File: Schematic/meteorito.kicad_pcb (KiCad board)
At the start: 2 copper layers, 95.3 x 89.4 mm, 17 parts, among them P1 DH22, P10 CONN_01X10, P2 GY-ML8511, P3 BMP180, P4 Hall, P5 Hall, P6 Hall, P7 CONN_01X10, P8 CONN_01X10, P9 CONN_01X10

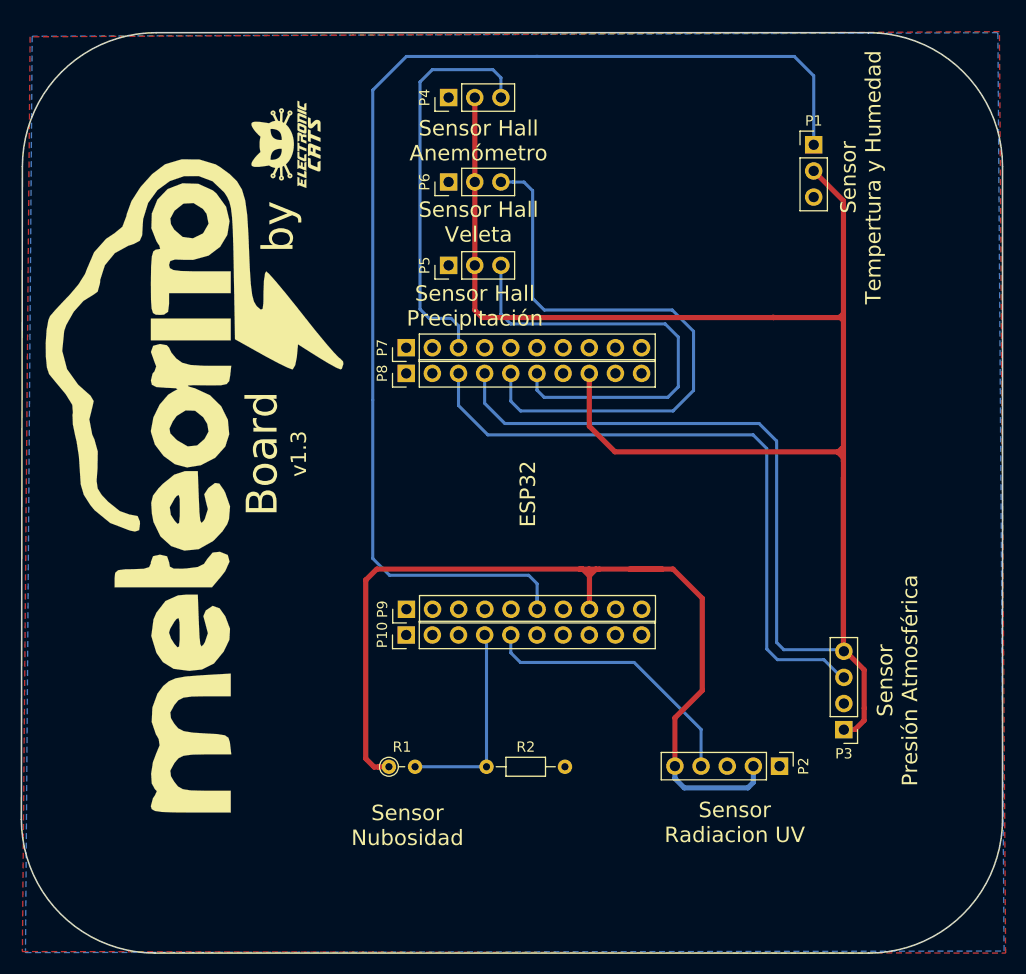
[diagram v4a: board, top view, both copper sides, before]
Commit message: Add library update components and layout
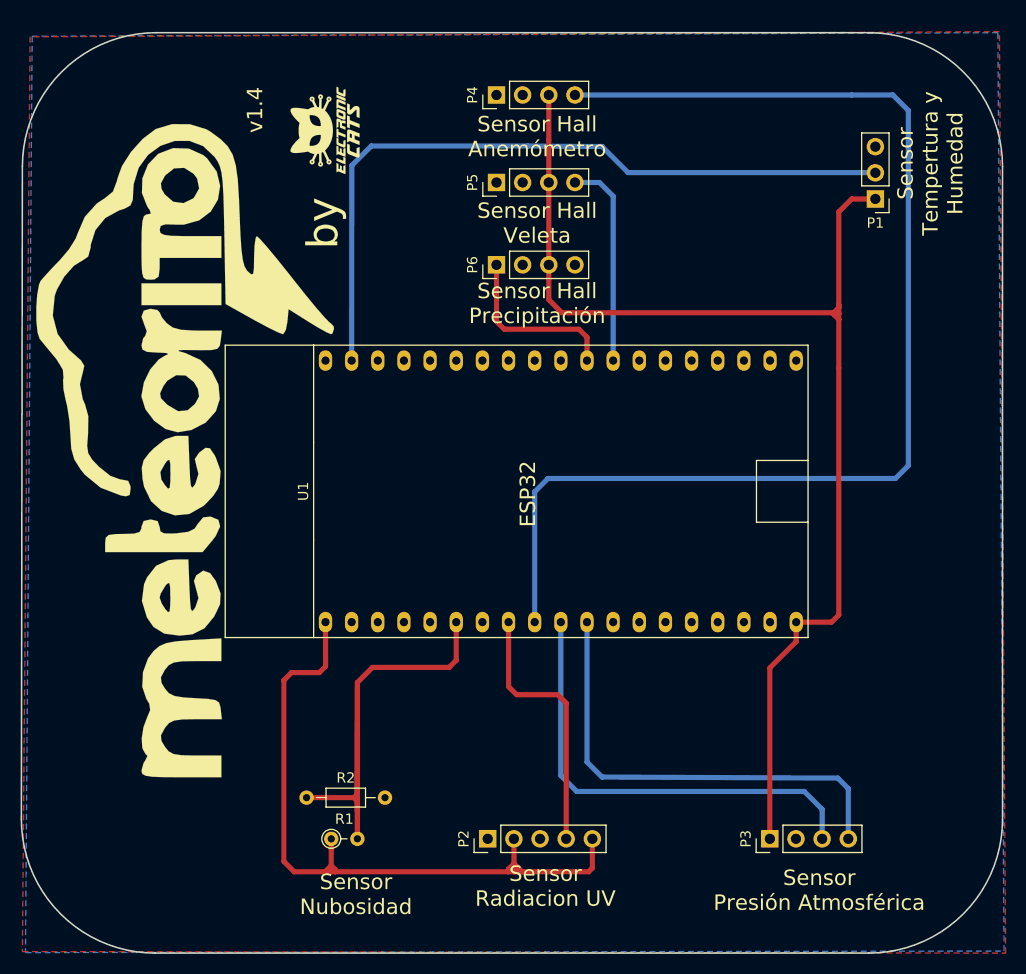
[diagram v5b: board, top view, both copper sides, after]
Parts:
- removed P10, P7, P8, P9: CONN_01X10, Connector_PinHeader_2.54mm:PinHeader_1x10_P2.54mm_Vertical
- added U1: ESP32-DEVKIT, meteorito:ESP32-DEVKIT, F.Cu at (92.1, 100.2)
- P4: value Hall -> Velocidad; footprint Connector_PinHeader_2.54mm:PinHeader_1x03_P2.54mm_Vertical -> Connector_PinHeader_2.54mm:PinHeader_1x04_P2.54mm_Vertical
- P5, P6: value Hall -> Precipitacion; footprint Connector_PinHeader_2.54mm:PinHeader_1x03_P2.54mm_Vertical -> Connector_PinHeader_2.54mm:PinHeader_1x04_P2.54mm_Vertical
- moved P2 29.2 mm to (85.0, 134.0), turned to 90 degrees
- moved R2 17.7 mm to (67.4, 130.0)
- moved P3 12.8 mm to (112.4, 134.0), turned to 90 degrees
- moved P5 9.30 mm to (85.8, 70.2)
- moved P6 9.30 mm to (85.8, 78.2)
- moved R1 8.96 mm to (69.8, 134.0)
- moved P1 7.97 mm to (122.7, 71.8), turned to 180 degrees
- moved P4 4.66 mm to (85.8, 61.8)
- moved G*** 4.03 mm to (69.2, 65.2)
- moved G*** 3.54 mm to (55.6, 96.3)
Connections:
- P1 pad 1: /IO23 -> +5V
- P1 pad 2: +5V -> /DHT22
- P2 pad 4: /IO33 -> /UV-SENSOR
- P3 pad 3: /IO22 -> /SCL
- P3 pad 4: /IO21 -> /SDA
- P4 pad 1: GND -> Net-(P4-Pad1)
- P4 pad 2: +5V -> GND
- P4 pad 3: /IO25 -> +5V
- P5 pad 1: GND -> Net-(P5-Pad1)
- P5 pad 2: +5V -> GND
- P5 pad 3: /IO16 -> +5V
- P6 pad 1: GND -> /IO17
- P6 pad 2: +5V -> GND
- P6 pad 3: /IO17 -> +5V
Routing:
- net /IO23: track 118.1 -> 0.00 mm
- net /AIRE-HALL: track 0.00 -> 117.5 mm
- net /DHT22: track 0.00 -> 71.3 mm
- net /IO22: track 62.6 -> 0.00 mm
- net /IO21: track 59.0 -> 0.00 mm
- net /SDA: track 0.00 -> 44.9 mm
- net /SCL: track 0.00 -> 44.5 mm
- net +5V: track 163.2 -> 120.2 mm
- net /IO17: track 58.2 -> 17.2 mm
- net /IO25: track 39.2 -> 0.00 mm
- net /IO35: track 19.8 -> 51.1 mm
- net /IO33: track 26.9 -> 0.00 mm
- net /UV-SENSOR: track 0.00 -> 25.7 mm
- net /IO16: track 43.8 -> 20.2 mm
- net +3V3: track 92.2 -> 70.1 mm
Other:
- net class Default: clearance 0.2 -> 0.4; trace_width 0.3 -> 0.5
- net class Voltaje: clearance 0.2 -> 0.4
- rule trace_clearance: 0.2 -> 0.4
- board text added: "v1.4"
- board text removed: "Board"
- board text removed: "v1.3"

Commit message: Add labels pins
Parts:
- moved G*** 2.16 mm to (127.5, 116.6)
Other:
- board text added: "3V3"
- board text added: "5V"
- board text added: "A0"
- board text added: "D0"
- board text added: "FOTORESISTENCIA"
- board text added: "GND"
- board text added: "NC"
- board text added: "PIN"
- board text added: "SCL"
- board text added: "SDA"
- board text added: "UV"
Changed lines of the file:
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@@
   (general
     (thickness 1.6)
-    (drawings 29)
+    (drawings 53)
     (tracks 103)
     (zones 0)
@@
   )
   (module Aesthetics:hacedores (layer B.Cu)
-    (at 125.349 116.713 270)
+    (at 127.508 116.586 270)
     (fp_text reference G*** (at 0 0 270) (layer B.SilkS) hide
       (effects (font (size 1.524 1.524) (thickness 0.3)) (justify mirror))
@@
       (xy -20.493307 -10.275275) (xy -20.495908 -10.265513)) (layer B.SilkS) (width 0))
   )
+  (gr_text NC (at 85.598 64.008) (layer B.SilkS)
+    (effects (font (size 1 1) (thickness 0.15)) (justify mirror))
+  )
+  (gr_text NC (at 85.598 72.39) (layer B.SilkS)
+    (effects (font (size 1 1) (thickness 0.15)) (justify mirror))
+  )
+  (gr_text NC (at 93.218 80.518) (layer B.SilkS)
+    (effects (font (size 1 1) (thickness 0.15)) (justify mirror))
+  )
+  (gr_text FOTORESISTENCIA (at 71.12 136.398) (layer B.SilkS)
+    (effects (font (size 1 1) (thickness 0.15)) (justify mirror))
+  )
+  (gr_text 3V3 (at 87.63 131.318 90) (layer B.SilkS)
+    (effects (font (size 1 1) (thickness 0.15)) (justify mirror))
+  )
+  (gr_text GND (at 90.17 131.318 90) (layer B.SilkS)
+    (effects (font (size 1 1) (thickness 0.15)) (justify mirror))
+  )
+  (gr_text UV (at 92.71 131.572 90) (layer B.SilkS)
+    (effects (font (size 1 1) (thickness 0.15)) (justify mirror))
+  )
+  (gr_text 3V3 (at 95.25 131.318 90) (layer B.SilkS)
+    (effects (font (size 1 1) (thickness 0.15)) (justify mirror))
+  )
+  (gr_text 5V (at 112.522 131.572 90) (layer B.SilkS)
+    (effects (font (size 1 1) (thickness 0.15)) (justify mirror))
+  )
+  (gr_text GND (at 115.062 131.318 90) (layer B.SilkS)
+    (effects (font (size 1 1) (thickness 0.15)) (justify mirror))
+  )
+  (gr_text SDA (at 119.888 131.064 90) (layer B.SilkS)
+    (effects (font (size 1 1) (thickness 0.15)) (justify mirror))
+  )
+  (gr_text SCL (at 117.348 131.318 90) (layer B.SilkS)
+    (effects (font (size 1 1) (thickness 0.15)) (justify mirror))
+  )
+  (gr_text 5V (at 119.888 71.882) (layer B.SilkS)
+    (effects (font (size 1 1) (thickness 0.15)) (justify mirror))
+  )
+  (gr_text PIN (at 119.888 69.342) (layer B.SilkS)
+    (effects (font (size 1 1) (thickness 0.15)) (justify mirror))
+  )
+  (gr_text GND (at 119.634 66.802) (layer B.SilkS)
+    (effects (font (size 1 1) (thickness 0.15)) (justify mirror))
+  )
+  (gr_text 5V (at 90.932 80.518) (layer B.SilkS)
+    (effects (font (size 1 1) (thickness 0.15)) (justify mirror))
+  )
+  (gr_text GND (at 88.392 80.518) (layer B.SilkS)
+    (effects (font (size 1 1) (thickness 0.15)) (justify mirror))
+  )
+  (gr_text D0 (at 85.852 80.518) (layer B.SilkS)
+    (effects (font (size 1 1) (thickness 0.15)) (justify mirror))
+  )
+  (gr_text GND (at 88.392 72.39) (layer B.SilkS)
+    (effects (font (size 1 1) (thickness 0.15)) (justify mirror))
+  )
+  (gr_text 5V (at 90.932 72.39) (layer B.SilkS)
+    (effects (font (size 1 1) (thickness 0.15)) (justify mirror))
+  )
+  (gr_text A0 (at 93.472 72.39) (layer B.SilkS)
+    (effects (font (size 1 1) (thickness 0.15)) (justify mirror))
+  )
+  (gr_text GND (at 88.392 64.008) (layer B.SilkS)
+    (effects (font (size 1 1) (thickness 0.15)) (justify mirror))
+  )
+  (gr_text 5V (at 90.932 64.008) (layer B.SilkS)
+    (effects (font (size 1 1) (thickness 0.15)) (justify mirror))
+  )
+  (gr_text A0 (at 93.472 64.008) (layer B.SilkS)
+    (effects (font (size 1 1) (thickness 0.15)) (justify mirror))
+  )
   (gr_text "Sensor Hall\nPrecipitación " (at 89.8 82) (layer F.SilkS)
     (effects (font (size 1.5 1.5) (thickness 0.3)))
@@
     (effects (font (size 2.5 2.5) (thickness 0.3)) (justify mirror))
   )
-  (gr_text "Con ayuda de:" (at 124.29236 81.67878 90) (layer B.SilkS)
+  (gr_text "Con ayuda de:" (at 126.238 81.534 90) (layer B.SilkS)
     (effects (font (size 2.5 2.5) (thickness 0.3)) (justify mirror))
   )
